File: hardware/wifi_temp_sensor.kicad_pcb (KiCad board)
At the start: 2 copper layers, 50.8 x 45.7 mm, 12 parts, among them J1 USB_B_Mini, J2 ESP8266, J3 TempSensor, J4 Prog, J5 Aux_I2C, SW1 BootMode, U2 AZ1117-3.3

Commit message: manual merge from esp32_msf_rcnotes
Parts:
- removed J1: USB_B_Mini, Connector_USB:USB_Micro-B_Molex-105017-0001
- removed J4: Prog, Connector_PinHeader_2.54mm:PinHeader_1x06_P2.54mm_Vertical
- removed J5: Aux_I2C, Connector_PinSocket_2.54mm:PinSocket_1x04_P2.54mm_Vertical
- added C10: 100nF, Capacitor_SMD:C_0603_1608Metric, F.Cu at (183.5, 35.6)
- added C11: 10uF, Capacitor_SMD:C_0805_2012Metric, F.Cu at (186.1, 35.2)
- added C12: 100nF, Capacitor_SMD:C_0603_1608Metric, B.Cu at (248.3, 93.7)
- added C6: 10uF, Capacitor_SMD:C_0805_2012Metric, B.Cu at (252.7, 102.9)
- added C7: 22pF, Capacitor_SMD:C_0603_1608Metric, F.Cu at (189.5, 90.8)
- added C8: 22pF, Capacitor_SMD:C_0603_1608Metric, F.Cu at (192.8, 90.8)
- added C9: 10uF, Capacitor_SMD:C_0805_2012Metric, F.Cu at (186.1, 90.8)
- added CHG1: LED_Small, LED_SMD:LED_0603_1608Metric, F.Cu at (198.8, 103.5)
- added D1: D_Schottky, Diode_SMD:D_0603_1608Metric, F.Cu at (212.1, 85.1)
- added F1: Polyfuse_Small, Fuse:Fuse_0603_1608Metric, F.Cu at (185.4, 94.0)
- added IC2: BQ21040DBVR, TI BQ21040:SOT95P280X145-6N, B.Cu at (245.1, 100.0)
- added LED1: LED_Small, LED_SMD:LED_0603_1608Metric, F.Cu at (201.9, 103.5)
- added P1: USB_C_Plug_USB2.0, Connector_USB:USB_C_Receptacle_Palconn_UTC16-G, F.Cu at (191.0, 101.5)
- added Q1: SSM6L09FUTE85LF, SamacSys_parts:SOT65P210X120-6N, B.Cu at (243.0, 58.9)
- added Q2: AO3401A, Package_TO_SOT_SMD:SOT-23, F.Cu at (213.4, 88.9)
- added Q3: BSS214NW, Package_TO_SOT_SMD:SOT-323_SC-70, B.Cu at (253.4, 97.2)
- added R1: 100K, Resistor_SMD:R_0603_1608Metric, B.Cu at (238.9, 55.9)
- added R10: 10k, Resistor_SMD:R_0603_1608Metric, F.Cu at (184.8, 43.8)
- added R11: 100K, Resistor_SMD:R_0402_1005Metric, B.Cu at (246.2, 60.4)
- added R12: 5.1K, Resistor_SMD:R_0603_1608Metric, F.Cu at (187.3, 94.0)
- added R13: 5.1K, Resistor_SMD:R_0603_1608Metric, F.Cu at (194.3, 94.0)
- added R14: 33R, Resistor_SMD:R_0603_1608Metric, F.Cu at (201.9, 99.7)
- added R15: 10k, Resistor_SMD:R_0603_1608Metric, F.Cu at (209.6, 39.4)
- added R16: 10k, Resistor_SMD:R_0603_1608Metric, F.Cu at (184.8, 45.7)
- added R19: 33K, Resistor_SMD:R_0603_1608Metric, B.Cu at (240.7, 93.7)
- added R2: 100K, Resistor_SMD:R_0603_1608Metric, B.Cu at (238.9, 58.4)
- added R20: 10K, Resistor_SMD:R_0603_1608Metric, B.Cu at (245.1, 93.7)
- added R21: 33R, Resistor_SMD:R_0603_1608Metric, F.Cu at (198.8, 99.9)
- added R3: 10k, Resistor_SMD:R_0603_1608Metric, F.Cu at (221.0, 37.2)
- added R4: 10k, Resistor_SMD:R_0603_1608Metric, F.Cu at (220.9, 35.2)
- added R5: 10K, Resistor_SMD:R_0603_1608Metric, F.Cu at (214.2, 93.5)
- added R6: 1K, Resistor_SMD:R_0603_1608Metric, F.Cu at (211.3, 92.7)
- added R9: R_Small, Resistor_SMD:R_0603_1608Metric, B.Cu at (240.7, 101.3)
- added SW2: SW_Push, Button_Switch_SMD:SW_SPST_B3U-3000P, F.Cu at (208.7, 104.1)
- added U1: ESP32-C3-WROOM-02, PCM_Espressif:ESP32-C3-WROOM-02, F.Cu at (197.2, 42.2)
- added U3: WE-TVS-82400102, Package_TO_SOT_SMD:SOT-23-6, F.Cu at (191.1, 94.0)
- added U4: LD1117S33TR_SOT223, Package_TO_SOT_SMD:SOT-223-3_TabPin2, F.Cu at (221.6, 85.1)
- C1: value 10uF -> 1uF; footprint Capacitor_SMD:C_1206_3216Metric -> Capacitor_SMD:C_0603_1608Metric
- C2: value 22uF -> 10uF; footprint Capacitor_SMD:C_1206_3216Metric -> Capacitor_SMD:C_0805_2012Metric
- C3: value C_Small -> 1uF; footprint Capacitor_SMD:C_1206_3216Metric -> Capacitor_SMD:C_0603_1608Metric; moved to B.Cu
- C4: value C_Small -> 100nF; footprint Capacitor_SMD:C_1206_3216Metric -> Capacitor_SMD:C_0603_1608Metric; moved to B.Cu
- C5: value C_Small -> 100nF; footprint Capacitor_SMD:C_1206_3216Metric -> Capacitor_SMD:C_0402_1005Metric
- J2: value ESP8266 -> Batt_Conn; footprint Connector_PinSocket_2.54mm:PinSocket_2x04_P2.54mm_Vertical -> Connector_JST:JST_ACH_BM02B-ACHSS-GAN-ETF_1x02-1MP_P1.20mm_Vertical; moved to B.Cu
- J3: value TempSensor -> Conn_02x03_Odd_Even; footprint Connector_PinSocket_2.54mm:PinSocket_1x04_P2.54mm_Vertical -> Connector_PinHeader_1.27mm:PinHeader_2x03_P1.27mm_Vertical
- SW1: value BootMode -> SW_SPST; footprint Button_Switch_THT:SW_PUSH_6mm -> Button_Switch_SMD:SW_SPDT_CK-JS102011SAQN
- U2: value AZ1117-3.3 -> SHT4x; footprint Package_TO_SOT_SMD:SOT-89-3 -> Sensor_Humidity:Sensirion_DFN-4_1.5x1.5mm_P0.8mm_SHT4x_NoCentralPad
- moved SW1 67.6 mm to (219.3, 103.8), turned to 0 degrees
- moved C3 59.5 mm to (240.7, 97.5)
- moved C1 42.9 mm to (214.6, 85.1)
- moved C2 42.6 mm to (224.2, 90.2), turned to 180 degrees
- moved C4 41.3 mm to (242.9, 53.3), turned to 180 degrees
- moved J2 34.2 mm to (225.4, 95.2), turned to 0 degrees
- moved C5 22.6 mm to (226.2, 38.1), turned to 0 degrees
- moved U2 13.9 mm to (226.5, 36.0), turned to -90 degrees
- moved J3 10.8 mm to (212.7, 43.5), turned to 0 degrees
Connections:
- C1 pad 1: +5V -> Net-(D1-K)
- C3 pad 1: +3.3V -> V_USB
- C4 pad 1: GND -> V_BAT_MEAS
- C4 pad 2: +3.3V -> GND
- J2 pad 2: ESP_Tx -> Net-(J2-Pin_2)
- J3 pad 1: +3.3V -> EN
- J3 pad 2: GND -> +3.3V
- J3 pad 3: SCL -> TXD
- J3 pad 4: SDA -> IO9
- SW1 pad 1: SCL -> Net-(J2-Pin_2)
- SW1 pad 2: GND -> V_BAT
- U2 pad 1: GND -> SDA
- U2 pad 2: +3.3V -> SDC
- U2 pad 3: +5V -> +3.3V
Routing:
- net SCL: track 58.5 -> 0.00 mm
- net D+: track 0.00 -> 57.6 mm
- net D-: track 0.00 -> 56.9 mm
- net +3.3V: track 55.6 -> 0.00 mm, vias 2 -> 0
- net SDA: track 42.2 -> 0.00 mm
- net +5V: track 27.7 -> 0.00 mm
- net GND: track 30.0 -> 11.8 mm, vias 16 -> 8
- net ESP_Rx: track 16.9 -> 0.00 mm
- net Net-(F1-Pad1): track 0.00 -> 13.8 mm, vias 0 -> 2
- net unconnected-(J1-Shield-Pad6): track 13.2 -> 0.00 mm
- net ESP_Tx: track 12.5 -> 0.00 mm
- net V_USB: track 0.00 -> 9.96 mm
- net Net-(P1-CC): track 0.00 -> 5.67 mm
- net Net-(P1-VCONN): track 0.00 -> 4.83 mm
- net Net-(P1-D-): track 0.00 -> 4.22 mm
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- removed copper zone on F.Cu, net +3.3V
- removed copper zone on B.Cu, net GND
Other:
- board size 50.8 x 45.7 mm -> 50 x 77 mm

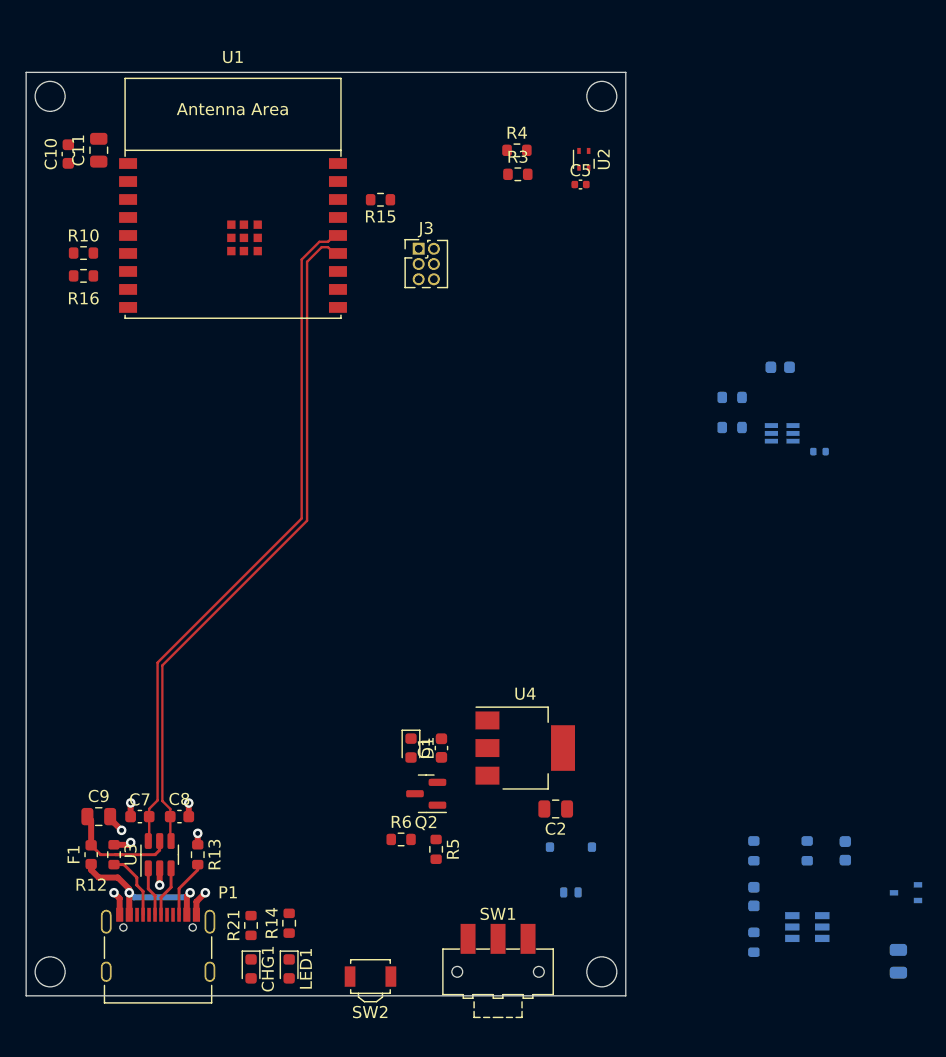
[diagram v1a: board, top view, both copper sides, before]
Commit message: finished initial PCB layout
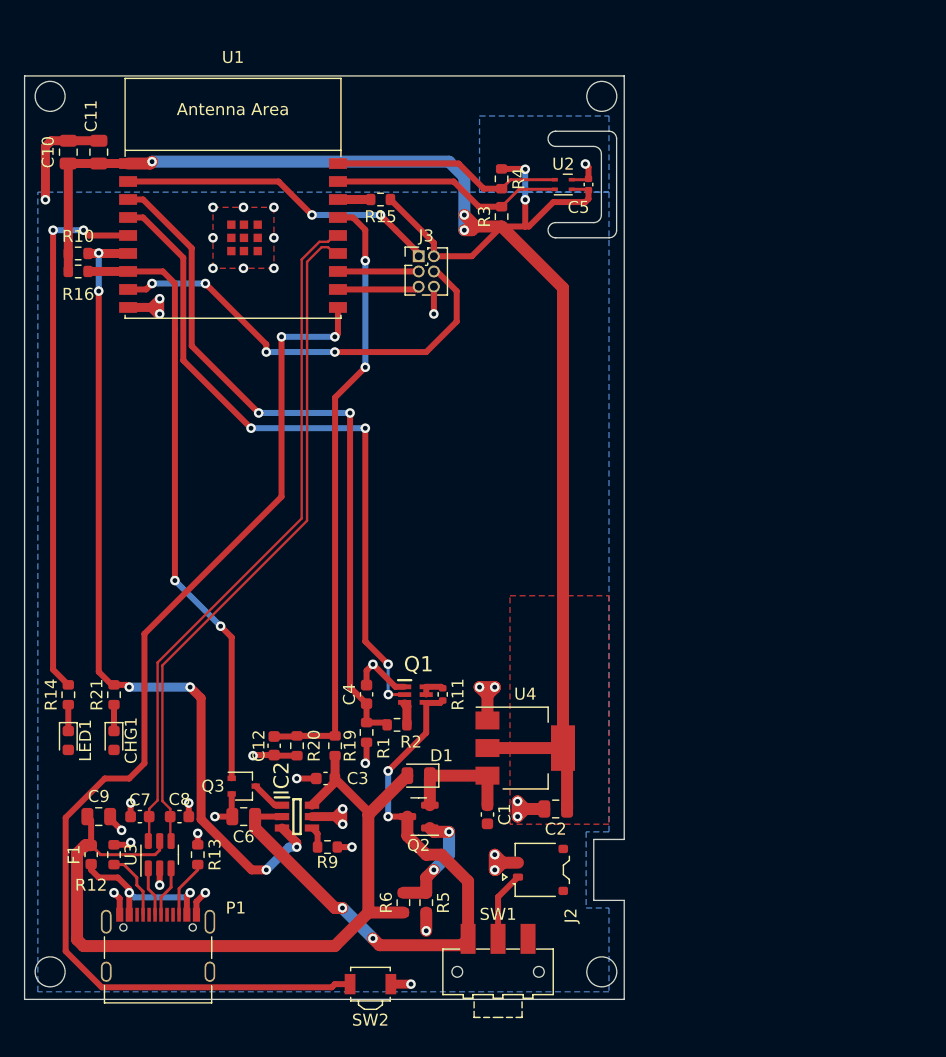
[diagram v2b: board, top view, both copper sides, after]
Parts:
- C10: footprint Capacitor_SMD:C_0603_1608Metric -> Capacitor_SMD:C_0805_2012Metric
- C12, C3, C4, C6, IC2, J2, Q1, Q3, R1, R11, R19, R2, R20, R9: moved to F.Cu
- D1: footprint Diode_SMD:D_0603_1608Metric -> Diode_SMD:D_0805_2012Metric
- moved Q3 55.9 mm to (198.1, 88.3), turned to 0 degrees
- moved C6 55.9 mm to (198.1, 90.8), turned to 180 degrees
- moved C12 48.4 mm to (200.7, 84.9)
- moved C4 44.0 mm to (208.4, 80.6), turned to 90 degrees
- moved IC2 43.5 mm to (202.6, 90.8), turned to 0 degrees
- moved R20 43.4 mm to (202.6, 84.9)
- moved R1 41.3 mm to (208.4, 83.8), turned to -90 degrees
- moved Q1 37.5 mm to (212.5, 80.6), turned to 0 degrees
- moved R11 37.4 mm to (214.7, 80.6), turned to 90 degrees
- moved R2 37.4 mm to (210.9, 83.2)
- moved C3 37.1 mm to (205.0, 87.6), turned to 180 degrees
- moved R9 36.4 mm to (205.1, 93.3), turned to 0 degrees
- moved R19 36.0 mm to (205.8, 84.9)
- moved LED1 26.5 mm to (183.5, 84.5)
- moved R14 26.5 mm to (183.5, 80.6)
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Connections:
- J2 pad 1: GND -> Net-(J2-Pin_1)
- J2 pad 2: Net-(J2-Pin_2) -> GND
- R21 pad 2: ~{CRG} -> ~{CHG}
- SW1 pad 1: Net-(J2-Pin_2) -> V_BAT
- SW1 pad 2: V_BAT -> Net-(J2-Pin_1)
- SW2 pad 1: UTIL -> GND
- SW2 pad 2: GND -> UTIL
- U1 pad 17: SDA -> SDC
- U1 pad 18: SDC -> SDA
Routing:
- net +3.3V: track 0.00 -> 138.8 mm, vias 0 -> 5
- net UTIL: track 0.00 -> 92.0 mm, vias 0 -> 2
- net ~{CHG}: track 0.00 -> 70.4 mm, vias 0 -> 6
- net GND: track 11.8 -> 70.7 mm, vias 8 -> 37
- net V_BAT_MEAS: track 0.00 -> 58.8 mm, vias 0 -> 2
- net V_USB: track 9.96 -> 68.8 mm
- net VBAT_MEAS_EN: track 0.00 -> 56.4 mm, vias 0 -> 4
- net V_BAT: track 0.00 -> 52.1 mm, vias 0 -> 4
- net V_USB_MEAS: track 0.00 -> 51.0 mm, vias 0 -> 2
- net CHG_ENABLE: track 0.00 -> 50.9 mm, vias 0 -> 2
- net ~{LED}: track 0.00 -> 44.9 mm, vias 0 -> 2
- net IO9: track 0.00 -> 36.5 mm, vias 0 -> 4
- net EN: track 0.00 -> 27.0 mm, vias 0 -> 2
- net SDC: track 0.00 -> 19.6 mm
- net SDA: track 0.00 -> 19.3 mm
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- added copper zone on F.Cu, net +3.3V
- added copper zone on B.Cu, net GND
- added copper zone on F.Cu, net GND
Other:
- outline, holes or cut-outs redrawn

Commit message: Small corrections
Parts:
- Q1: footprint SamacSys_parts:SOT65P210X120-6N -> SSM6N17FUTE85L:TRANS_SSM6N17FU_TE85L_F_
- U1: footprint PCM_Espressif:ESP32-C3-WROOM-02 -> Espressif:ESP32-C3-WROOM-02
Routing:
- net GND: track 70.7 -> 75.2 mm
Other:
- outline, holes or cut-outs redrawn
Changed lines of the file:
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@@
     (property "ki_description" "0.8A Single Input Single-Cell Li-Ion and Li-Pol Battery Charger")
     (attr smd)
-    (fp_text reference "IC2" (at -1.29 -3.175 90) (layer "F.SilkS")
+    (fp_text reference "IC2" (at 0 0) (layer "F.SilkS")
         (effects (font (size 1.27 1.27) (thickness 0.254)))
     )
@@
     )
   )
-  (footprint "SamacSys_parts:SOT65P210X120-6N" (layer "F.Cu")
+  (footprint "SSM6N17FUTE85L:TRANS_SSM6N17FU_TE85L_F_" (layer "F.Cu")
     (at 212.46 80.63)
-    (descr "6lead")
-    (tags "MOSFET (N-Channel)")
     (property "Height" "1.2")
     (property "Manufacturer_Name" "Toshiba")
@@
     (property "ki_description" "MOSFET N-Ch P-Ch Sg FET 0.4A -0.2A 30V -30V")
     (attr smd)
-    (fp_text reference "Q1" (at 0.265 -2.525) (layer "F.SilkS")
-        (effects (font (size 1.27 1.27) (thickness 0.254)))
-    )
-    (fp_text value "SSM6L09FUTE85LF" (at 0 0) (layer "F.SilkS") hide
-        (effects (font (size 1.27 1.27) (thickness 0.254)))
-    )
-    (fp_text user "${REFERENCE}" (at 0 0) (layer "F.Fab")
-        (effects (font (size 1.27 1.27) (thickness 0.254)))
-    )
-    (fp_line (start -1.45 -1.2) (end -0.35 -1.2)
-      (stroke (width 0.2) (type solid)) (layer "F.SilkS"))
-    (fp_line (start -1.7 -1.35) (end 1.7 -1.35)
-      (stroke (width 0.05) (type solid)) (layer "F.CrtYd"))
-    (fp_line (start -1.7 1.35) (end -1.7 -1.35)
-      (stroke (width 0.05) (type solid)) (layer "F.CrtYd"))
-    (fp_line (start 1.7 -1.35) (end 1.7 1.35)
-      (stroke (width 0.05) (type solid)) (layer "F.CrtYd"))
-    (fp_line (start 1.7 1.35) (end -1.7 1.35)
-      (stroke (width 0.05) (type solid)) (layer "F.CrtYd"))
+    (fp_text reference "Q1" (at 0.057 -1.89) (layer "F.SilkS")
+        (effects (font (size 1 1) (thickness 0.15)))
+    )
+    (fp_text value "SSM6L09FUTE85LF" (at 7.7786 2.0534) (layer "F.Fab")
+        (effects (font (size 0.64 0.64) (thickness 0.15)))
+    )
+    (fp_line (start -0.625 -1.17) (end 0.625 -1.17)
+      (stroke (width 0.127) (type solid)) (layer "F.SilkS"))
+    (fp_line (start -0.625 1.17) (end 0.625 1.17)
+      (stroke (width 0.127) (type solid)) (layer "F.SilkS"))
+    (fp_circle (center -2.015 -0.85) (end -1.915 -0.85)
+      (stroke (width 0.2) (type solid)) (fill none) (layer "F.SilkS"))
+    (fp_line (start -1.6 -1.25) (end -1.6 1.25)
+      (stroke (width 0.05) (type solid)) (layer "F.CrtYd"))
+    (fp_line (start -1.6 -1.25) (end 1.6 -1.25)
+      (stroke (width 0.05) (type solid)) (layer "F.CrtYd"))
+    (fp_line (start -1.6 1.25) (end 1.6 1.25)
+      (stroke (width 0.05) (type solid)) (layer "F.CrtYd"))
+    (fp_line (start 1.6 -1.25) (end 1.6 1.25)
+      (stroke (width 0.05) (type solid)) (layer "F.CrtYd"))
+    (fp_line (start -0.625 -1) (end -0.625 1)
+      (stroke (width 0.127) (type solid)) (layer "F.Fab"))
     (fp_line (start -0.625 -1) (end 0.625 -1)
-      (stroke (width 0.1) (type solid)) (layer "F.Fab"))
-    (fp_line (start -0.625 -0.35) (end 0.025 -1)
-      (stroke (width 0.1) (type solid)) (layer "F.Fab"))
-    (fp_line (start -0.625 1) (end -0.625 -1)
-      (stroke (width 0.1) (type solid)) (layer "F.Fab"))
+      (stroke (width 0.127) (type solid)) (layer "F.Fab"))
+    (fp_line (start -0.625 1) (end 0.625 1)
+      (stroke (width 0.127) (type solid)) (layer "F.Fab"))
     (fp_line (start 0.625 -1) (end 0.625 1)
-      (stroke (width 0.1) (type solid)) (layer "F.Fab"))
-    (fp_line (start 0.625 1) (end -0.625 1)
-      (stroke (width 0.1) (type solid)) (layer "F.Fab"))
-    (pad "1" smd rect (at -0.9 -0.65 90) (size 0.4 1.1) (layers "F.Cu" "F.Paste" "F.Mask")
-      (net 1 "GND") (pinfunction "SOURCE_1") (pintype "passive"))
-    (pad "2" smd rect (at -0.9 0 90) (size 0.4 1.1) (layers "F.Cu" "F.Paste" "F.Mask")
-      (net 23 "VBAT_MEAS_EN") (pinfunction "GATE_1") (pintype "passive"))
-    (pad "3" smd rect (at -0.9 0.65 90) (size 0.4 1.1) (layers "F.Cu" "F.Paste" "F.Mask")
-      (net 24 "Net-(Q1-DRAIN_2)") (pinfunction "DRAIN_2") (pintype "passive"))
-    (pad "4" smd rect (at 0.9 0.65 90) (size 0.4 1.1) (layers "F.Cu" "F.Paste" "F.Mask")
-      (net 5 "V_BAT") (pinfunction "SOURCE_2") (pintype "passive"))
-    (pad "5" smd rect (at 0.9 0 90) (size 0.4 1.1) (layers "F.Cu" "F.Paste" "F.Mask")
-      (net 25 "Net-(Q1-DRAIN_1)") (pinfunction "GATE_2") (pintype "passive"))
-    (pad "6" smd rect (at 0.9 -0.65 90) (size 0.4 1.1) (layers "F.Cu" "F.Paste" "F.Mask")
-      (net 25 "Net-(Q1-DRAIN_1)") (pinfunction "DRAIN_1") (pintype "passive"))
+      (stroke (width 0.127) (type solid)) (layer "F.Fab"))
+    (fp_circle (center -2.015 -0.85) (end -1.915 -0.85)
+      (stroke (width 0.2) (type solid)) (fill none) (layer "F.Fab"))
+    (pad "1" smd rect (at -0.95 -0.65) (size 0.8 0.4) (layers "F.Cu" "F.Paste" "F.Mask")
+      (net 1 "GND") (pinfunction "SOURCE_1") (pintype "passive") (solder_mask_margin 0.102))
+    (pad "2" smd rect (at -0.95 0) (size 0.8 0.4) (layers "F.Cu" "F.Paste" "F.Mask")
+      (net 23 "VBAT_MEAS_EN") (pinfunction "GATE_1") (pintype "passive") (solder_mask_margin 0.102))
+    (pad "3" smd rect (at -0.95 0.65) (size 0.8 0.4) (layers "F.Cu" "F.Paste" "F.Mask")
+      (net 24 "Net-(Q1-DRAIN_2)") (pinfunction "DRAIN_2") (pintype "passive") (solder_mask_margin 0.102))
+    (pad "4" smd rect (at 0.95 0.65) (size 0.8 0.4) (layers "F.Cu" "F.Paste" "F.Mask")
+      (net 5 "V_BAT") (pinfunction "SOURCE_2") (pintype "passive") (solder_mask_margin 0.102))
+    (pad "5" smd rect (at 0.95 0) (size 0.8 0.4) (layers "F.Cu" "F.Paste" "F.Mask")
+      (net 25 "Net-(Q1-DRAIN_1)") (pinfunction "GATE_2") (pintype "passive") (solder_mask_margin 0.102))
+    (pad "6" smd rect (at 0.95 -0.65) (size 0.8 0.4) (layers "F.Cu" "F.Paste" "F.Mask")
+      (net 25 "Net-(Q1-DRAIN_1)") (pinfunction "DRAIN_1") (pintype "passive") (solder_mask_margin 0.102))
   )
   (footprint "Resistor_SMD:R_0402_1005Metric" (layer "F.Cu")
@@
     )
   )
-  (footprint "PCM_Espressif:ESP32-C3-WROOM-02" locked (layer "F.Cu")
+  (footprint "Espressif:ESP32-C3-WROOM-02" locked (layer "F.Cu")
     (at 197.25 42.25)
     (descr "ESP32-C3-WROOM-02: https://www.espressif.com/sites/default/files/documentation/esp32-c3-wroom-02_datasheet_en.pdf")
@@
   (gr_arc (start 227.33 34.925) (mid 227.779013 35.110987) (end 227.965 35.56)
     (stroke (width 0.1) (type default)) (layer "Edge.Cuts"))
-  (gr_circle (center 182 30.75) (end 183.25 30.75)
+  (gr_circle (center 182.41 31.585) (end 183.66 31.585)
     (stroke (width 0.1) (type default)) (fill none) (layer "Edge.Cuts"))
   (gr_line (start 229.235 34.29) (end 229.235 41.91)
@@
   (gr_arc (start 227.965 40.64) (mid 227.779013 41.089013) (end 227.33 41.275)
     (stroke (width 0.1) (type default)) (layer "Edge.Cuts"))
-  (gr_circle (center 182 103.75) (end 182 102.5)
+  (gr_circle (center 182.41 103.505) (end 183.66 103.505)
     (stroke (width 0.1) (type default)) (fill none) (layer "Edge.Cuts"))
   (gr_line (start 229.87 92.71) (end 229.87 29.045)
@@
   (gr_line (start 179.87 29.045) (end 229.87 29.045)
     (stroke (width 0.1) (type default)) (layer "Edge.Cuts"))
-  (gr_circle (center 228 103.75) (end 228 102.5)
+  (gr_circle (center 227.33 103.485) (end 227.33 102.235)
     (stroke (width 0.1) (type default)) (fill none) (layer "Edge.Cuts"))
   (gr_line (start 229.87 106.045) (end 179.87 106.045)
@@
   (gr_line (start 229.87 92.71) (end 227.33 92.71)
     (stroke (width 0.1) (type default)) (layer "Edge.Cuts"))
-  (gr_circle (center 228 30.75) (end 228 29.5)
+  (gr_circle (center 227.33 31.585) (end 228.58 31.585)
     (stroke (width 0.1) (type default)) (fill none) (layer "Edge.Cuts"))
   (gr_line (start 179.87 106.045) (end 179.87 29.045)
@@
   (via (at 194.945 97.155) (size 0.8) (drill 0.4) (layers "F.Cu" "B.Cu") (net 1))
   (via (at 206.395 91.44) (size 0.8) (drill 0.4) (layers "F.Cu" "B.Cu") (free) (net 1))
+  (segment (start 226.63 40.07) (end 226.06 40.64) (width 0.5) (layer "B.Cu") (net 1))
+  (segment (start 226.63 36.39) (end 226.63 40.07) (width 0.5) (layer "B.Cu") (net 1))
   (segment (start 184.245 93.892501) (end 184.245 101.06) (width 1) (layer "F.Cu") (net 2))
   (segment (start 185.42 91.12) (end 185.105 90.805) (width 0.5) (layer "F.Cu") (net 2))
@@
       )
     )
-  )
-  (zone (net 1) (net_name "GND") (layer "B.Cu") (hatch edge 0.5)
-    (priority 2)
-    (connect_pads (clearance 0.5))
-    (min_thickness 0.25) (filled_areas_thickness no)
-    (fill yes (thermal_gap 0.5) (thermal_bridge_width 0.5))
-    (polygon
-      (pts
-        (xy 228.6 32.385)
-        (xy 228.6 38.735)
-        (xy 217.805 38.735)
-        (xy 217.805 32.385)
-      )
-    )

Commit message: Added text to back of board
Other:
- board text added: "WiFi Temp Sensor - V1.0 Rich Clubb https://github.com/richClubb/wifi_temp_sensor"
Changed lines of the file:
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@@
   (gr_line (start 179.87 106.045) (end 179.87 29.045)
     (stroke (width 0.1) (type default)) (layer "Edge.Cuts"))
+  (gr_text "WiFi Temp Sensor - V1.0\nRich Clubb \nhttps://github.com/richClubb/wifi_temp_sensor" (at 185.42 30.48 180) (layer "B.SilkS")
+    (effects (font (size 1 1) (thickness 0.15)) (justify left bottom mirror))
+  )
   (segment (start 190.955 48.895) (end 190.41 48.35) (width 0.75) (layer "F.Cu") (net 1))
   (segment (start 188.531 93.155) (end 187.325 93.155) (width 0.5) (layer "F.Cu") (net 1))

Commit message: fixed a few small issues, connected 3.3v to LEDs
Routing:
- net +3.3V: track 138.8 -> 183.0 mm
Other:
- board text added: "Battery"
